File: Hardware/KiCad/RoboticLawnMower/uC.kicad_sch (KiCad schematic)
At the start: 20 parts, among them J12 Conn_02x05_Row_Letter_Last, U2 AVR128DB48x-xPT, U5 W25Q128JVS, Y1 32.768kHz

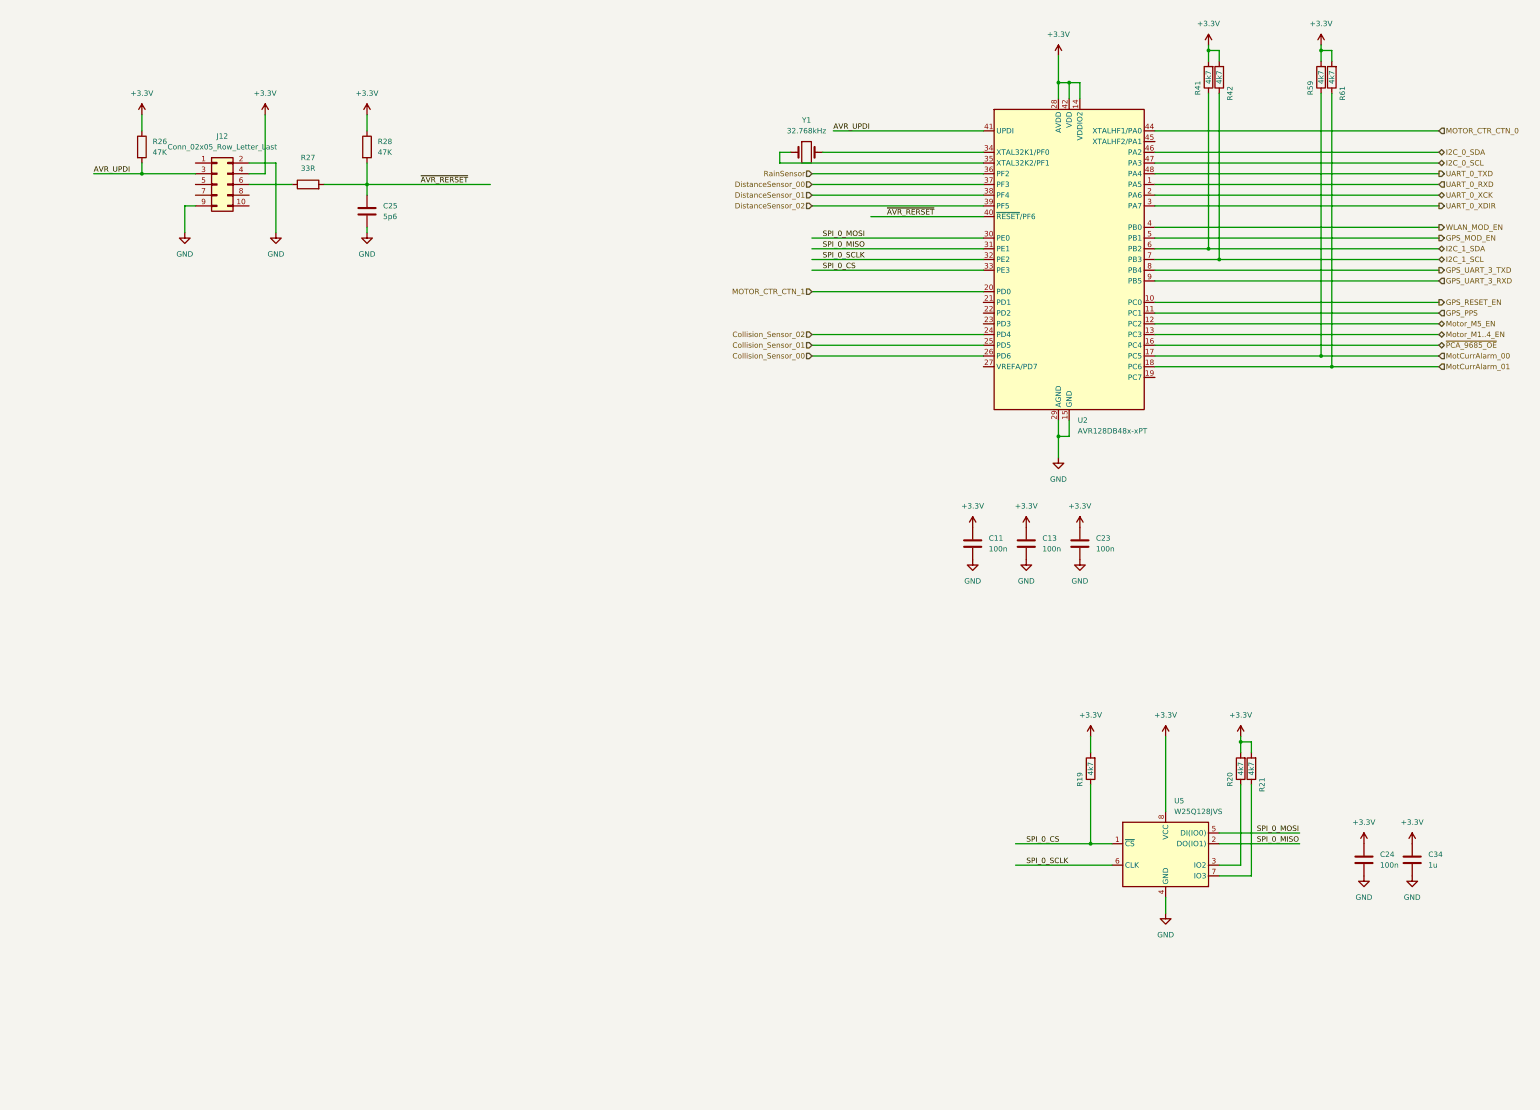
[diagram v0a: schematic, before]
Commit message: Redesign: - Controller - I2C pinning geändert - uvm
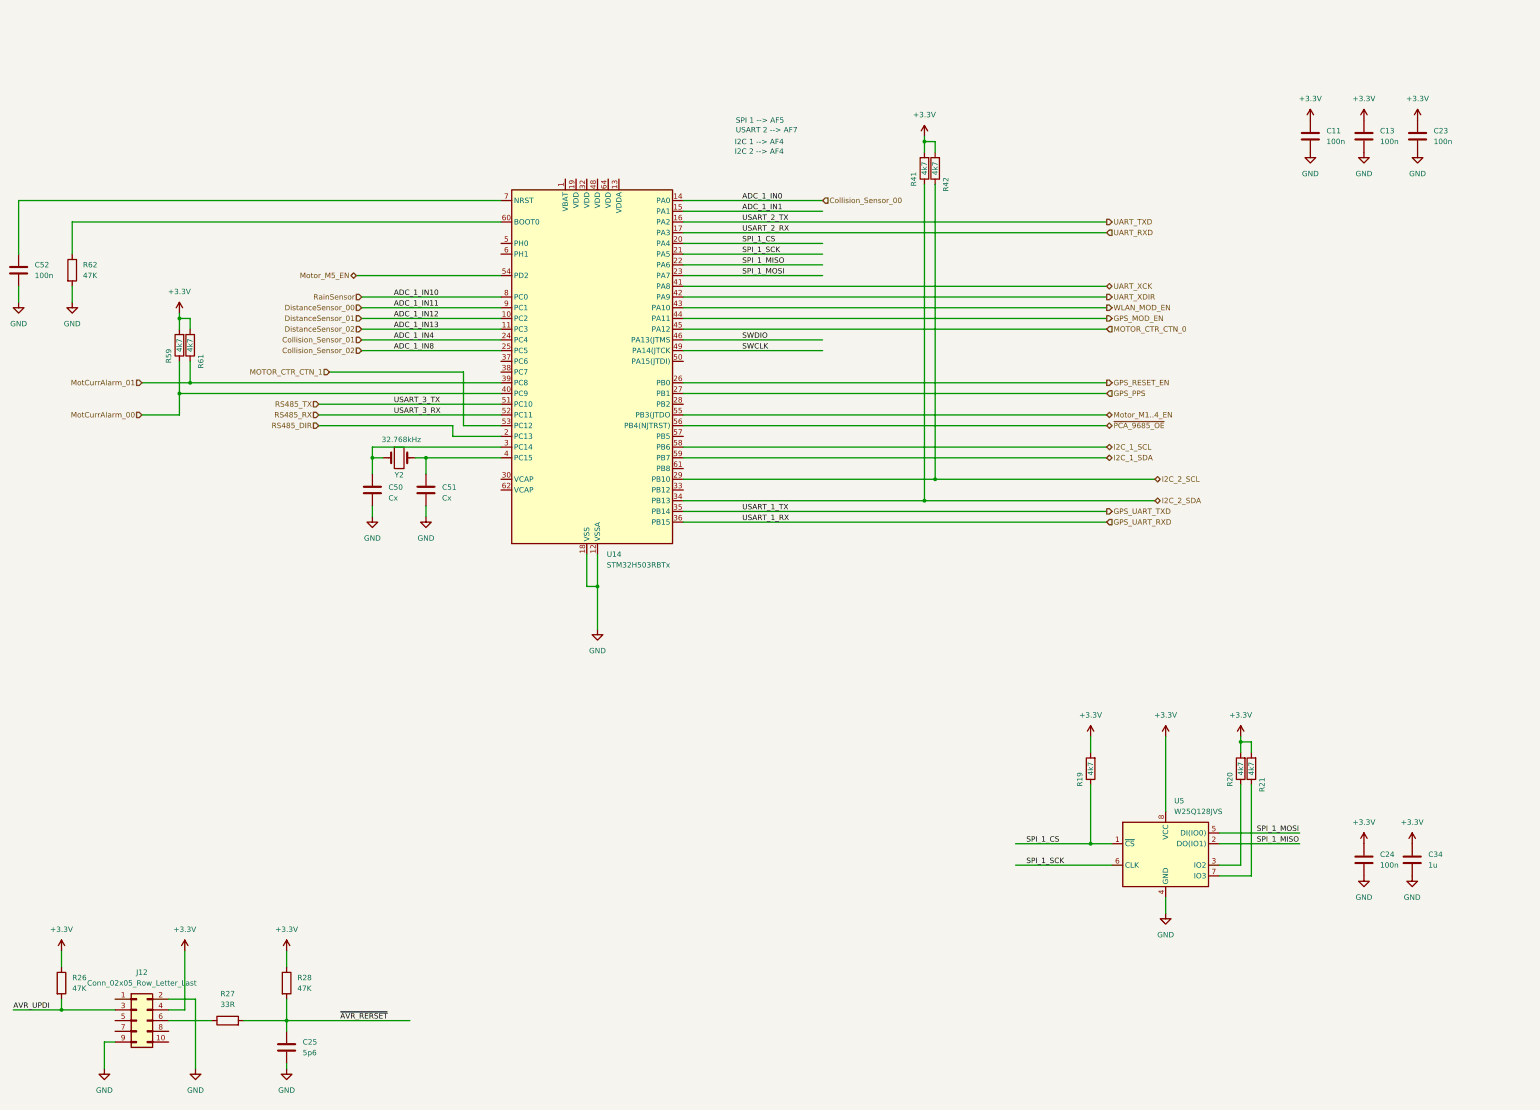
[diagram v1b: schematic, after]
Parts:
- removed U2: AVR128DB48x-xPT, Package_QFP:TQFP-48_7x7mm_P0.5mm, symbol MCU_Microchip_AVR_Dx:AVR128DB48x-xPT
- removed Y1: 32.768kHz, Crystal:Crystal_SMD_3215-2Pin_3.2x1.5mm, symbol Device:Crystal
- added C50, C51: Cx, Capacitor_SMD:C_0603_1608Metric, symbol Device:C
- added C52: 100n, Capacitor_SMD:C_0603_1608Metric, symbol Device:C
- added R62: 47K, Resistor_SMD:R_0603_1608Metric, symbol Device:R
- added U14: STM32H503RBTx, Package_QFP:LQFP-64_10x10mm_P0.5mm, symbol MCU_ST_STM32H5:STM32H503RBTx
- added Y2: 32.768kHz, Crystal:Crystal_SMD_3215-2Pin_3.2x1.5mm, symbol Device:Crystal
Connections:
- net Collision_Sensor_00: now also U14.14 (PA0)
- net Collision_Sensor_01: now also U14.24 (PC4)
- net Collision_Sensor_02: now also U14.25 (PC5)
- net DistanceSensor_00: now also U14.9 (PC1)
- net DistanceSensor_01: now also U14.10 (PC2)
- net DistanceSensor_02: now also U14.11 (PC3)
- net GND: now also C50.2, C51.2, C52.2, R62.2, U14.12 (VSSA), U14.18 (VSS), U14.31 (VSS), U14.47 (VSS), U14.63 (VSS)
- net GPS_MOD_EN: now also U14.44 (PA11)
- net GPS_PPS: now also U14.27 (PB1)
- net GPS_RESET_EN: now also U14.26 (PB0)
- net I2C_1_SCL: now also U14.58 (PB6); no longer R42.1
- net I2C_1_SDA: now also U14.59 (PB7); no longer R41.1
- net MOTOR_CTR_CTN_0: now also U14.45 (PA12)
- net MOTOR_CTR_CTN_1: now also U14.53 (PC12)
- net MotCurrAlarm_00: now also U14.40 (PC9)
- net MotCurrAlarm_01: now also U14.39 (PC8)
- net Motor_M1..4_EN: now also U14.55 (PB3(JTDO)
- net Motor_M5_EN: now also U14.54 (PD2)
- net RainSensor: now also U14.8 (PC0)
- net WLAN_MOD_EN: now also U14.43 (PA10)
- net ~{PCA_9685_OE}: now also U14.56 (PB4(NJTRST))
- net SPI_0_CS renamed SPI_1_CS
- net SPI_1_CS: now also U14.20 (PA4)
- net SPI_0_MISO renamed SPI_1_MISO
- net SPI_1_MISO: now also U14.22 (PA6)
- net SPI_0_MOSI renamed SPI_1_MOSI
- net SPI_1_MOSI: now also U14.23 (PA7)
- net SPI_0_SCLK renamed SPI_1_SCK
- net SPI_1_SCK: now also U14.21 (PA5)
- new net: C51.1, U14.4 (PC15), Y2.2
- new net: C50.1, U14.3 (PC14), Y2.1
- new net: R62.1, U14.60 (BOOT0)
- new net: C52.1, U14.7 (NRST)
- new net ADC_1_IN1: U14.15 (PA1)
- new net GPS_UART_RXD: U14.36 (PB15)
- new net GPS_UART_TXD: U14.35 (PB14)
- new net I2C_2_SCL: R42.1, U14.29 (PB10)
- new net I2C_2_SDA: R41.1, U14.34 (PB13)
- new net RS485_DIR: U14.2 (PC13)
- new net RS485_RX: U14.52 (PC11)
- new net RS485_TX: U14.51 (PC10)
- new net SWCLK: U14.49 (PA14(JTCK)
- new net SWDIO: U14.46 (PA13(JTMS)
- new net UART_RXD: U14.17 (PA3)
- new net UART_TXD: U14.16 (PA2)
- new net UART_XCK: U14.41 (PA8)
- new net UART_XDIR: U14.42 (PA9)
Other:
- note added: "I2C 1 --> AF4"
- note added: "I2C 2 --> AF4"
- note added: "SPI 1 --> AF5"
- note added: "USART 2 --> AF7"
- moved on the sheet: C11, C13, C23, C25, J12, R26, R27, R28, R41, R42, R59, R61

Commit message: change µC to STM32H573
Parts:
- added C40: 100n, Capacitor_SMD:C_0603_1608Metric, symbol Device:C
- added C41, C42: 10µ, Capacitor_SMD:C_0603_1608Metric, symbol Device:C
- U14: value STM32H503RBTx -> STM32H573RITx; symbol MCU_ST_STM32H5:STM32H503RBTx -> MCU_ST_STM32H5:STM32H573RITx
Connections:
- net +3.3V: now also U14.13 (VDDA), U14.19 (VDD), U14.32 (VDD), U14.48 (VDD), U14.64 (VDD), C40.1, C41.1, C42.1
- net GND: now also C40.2, C41.2, C42.2
- net MOT_SIG_5: now reaches U14.37 (PC6)

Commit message: Layout fertig, Gerber-Datei muss noch erzeugt werden.
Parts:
- removed C25: 5p6, Capacitor_SMD:C_0603_1608Metric, symbol Device:C
- removed R26, R28: 47K, Resistor_SMD:R_0603_1608Metric, symbol Device:R
- removed R27: 33R, Resistor_SMD:R_0603_1608Metric, symbol Device:R
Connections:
- net AVR_UPDI is gone; now on net GND: J12.3 (Pin_3)
- net +3.3V: now also J12.1 (Pin_1); no longer J12.4 (Pin_4)
- net GND: now also J12.5 (Pin_5); no longer J12.2 (Pin_2)
- net I2C_2_SDA: now also U14.33 (PB12); no longer U14.34 (PB13)
- net MOTOR_CTR_CTN_0: now also U14.50 (PA15(JTDI)); no longer U14.45 (PA12)
- net Motor_M1..4_EN: now also U14.57 (PB5); no longer U14.55 (PB3(JTDO)
- net Motor_M5_EN: now also U14.45 (PA12); no longer U14.54 (PD2)
- net SWCLK: now also J12.4 (Pin_4)
- net SWDIO: now also J12.2 (Pin_2)
- net NRST: now reaches J12.10 (Pin_10)
- net NRST: now also C52.1, U14.7 (NRST)
- net SWO: now reaches J12.6 (Pin_6)
- net SWO: now also U14.55 (PB3(JTDO)
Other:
- note added: "PC06 --> MOTOR M SIG --> TIM03_CH1 --> AF2 PC12 --> MOTOR 2 SIG --> TIM15_CH1 --> AF2 PA15 --> MOTOR 1 SIG --> TIM02_CH1 --> AF1"
- note added: "USART 1 --> GPS --> AF4 USART 2 --> WLAN --> AF7 USART 3 --> RS485 --> AF7"
- note removed: "USART 2 --> AF7"

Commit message: Levelshift für MotorSignal zum µC
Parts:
- added C25: 100n, Capacitor_SMD:C_0603_1608Metric, symbol Device:C
- added C43: 2µ2, Capacitor_SMD:C_0603_1608Metric, symbol Device:C
- added R26, R27: N.C., Resistor_SMD:R_0603_1608Metric, symbol Device:R
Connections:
- net +3.3V: now also R26.1, R27.1
- net GND: now also C25.2, C43.2
- net at R62.1, U14.60 (BOOT0): now also R27.2
- net at U14.1 (VBAT): now also R26.2
- net at U14.30 (VCAP): now also U14.62 (VCAP), C25.1, C43.1
